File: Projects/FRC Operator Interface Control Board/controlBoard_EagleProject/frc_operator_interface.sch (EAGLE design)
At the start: 41 parts, among them CN1 1uF, CN2 1uF, CN3 1uF, CN4 1uF, J1 AVR_SPI_PRG_6PTH, J2 ANALOGHEADER, J3 DIGITALIN, J4 DIGITALOUTPUTS, J5 PWMHEADER, J6 UE27BC54130-USB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

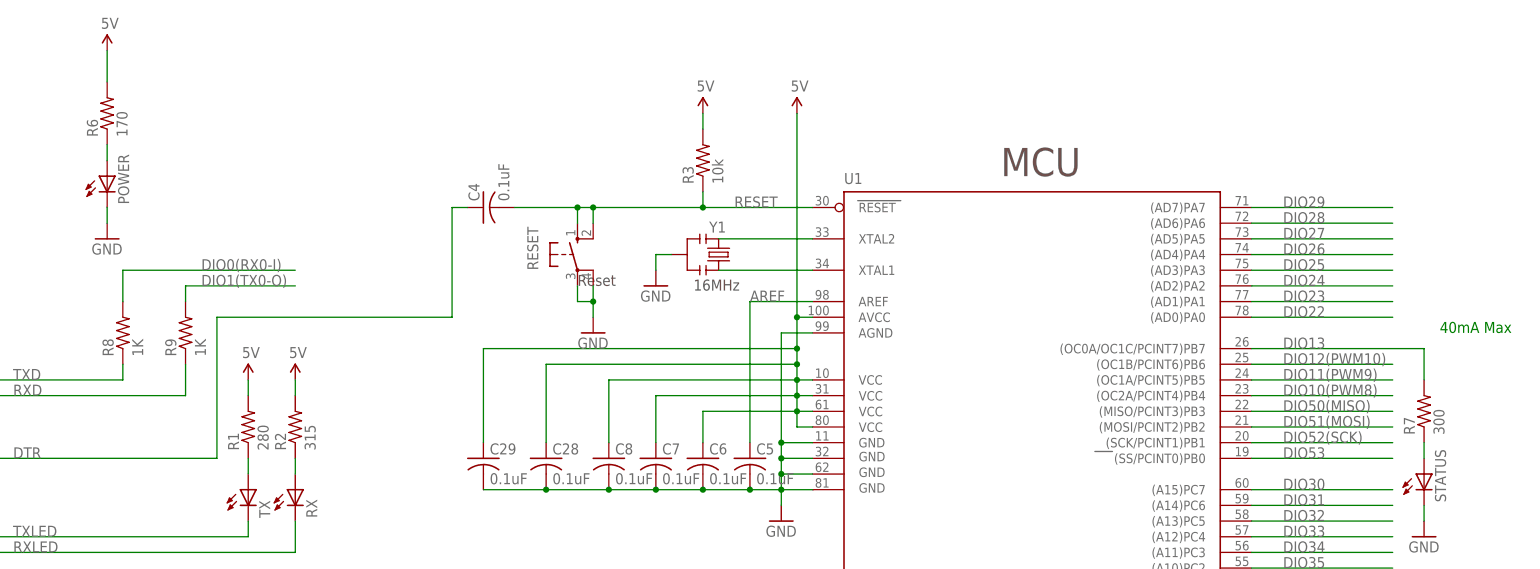
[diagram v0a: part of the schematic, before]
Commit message: Updated the resistor values for some of the LEDs on the board. Controller board code update commit.
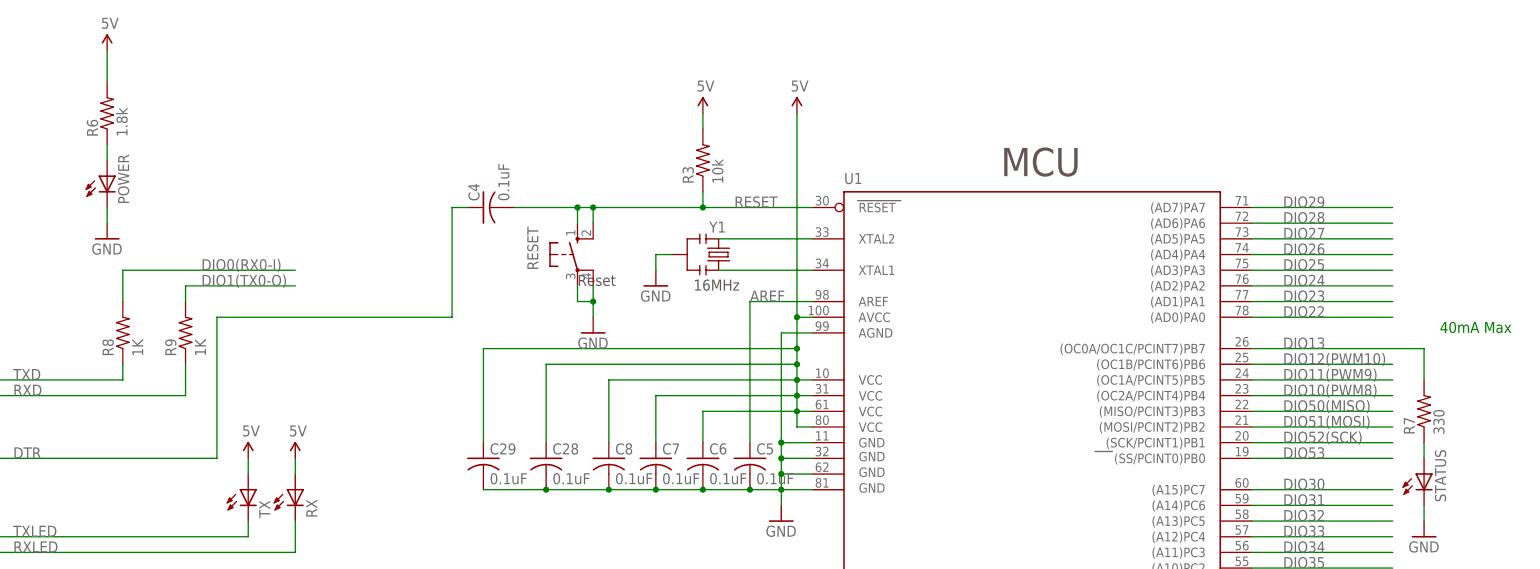
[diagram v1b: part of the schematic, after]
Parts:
- removed R1: 280, rcl:R-US_M1206
- removed R2: 315, rcl:R-US_M1206
- R6: value 170 -> 1.8k
- R7: value 300 -> 330
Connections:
- removed net N$1: R1.1, TX.A
- removed net N$5: R2.1, RX.A
- net 5V: now also RX.A, TX.A; no longer R1.2, R2.2
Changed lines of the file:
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@@
 <?xml version="1.0" encoding="utf-8"?>
 <!DOCTYPE eagle SYSTEM "eagle.dtd">
-<eagle version="6.5.0">
+<eagle version="7.5.0">
 <drawing>
 <settings>
@@
 <part name="C7" library="rcl" deviceset="C-US" device="C1206" value="0.1uF"/>
 <part name="C8" library="rcl" deviceset="C-US" device="C1206" value="0.1uF"/>
-<part name="R6" library="rcl" deviceset="R-US_" device="M1206" value="170"/>
+<part name="R6" library="rcl" deviceset="R-US_" device="M1206" value="1.8k"/>
 <part name="POWER" library="SparkFun-LED" deviceset="LED" device="3MM"/>
 <part name="GND12" library="SparkFun" deviceset="GND" device=""/>
-<part name="R7" library="rcl" deviceset="R-US_" device="M1206" value="300"/>
+<part name="R7" library="rcl" deviceset="R-US_" device="M1206" value="330"/>
 <part name="STATUS" library="SparkFun-LED" deviceset="LED" device="3MM"/>
 <part name="GND13" library="SparkFun" deviceset="GND" device=""/>
@@
 <part name="GND16" library="SparkFun" deviceset="GND" device=""/>
 <part name="U2" library="SparkFun" deviceset="FT232RL" device="SSOP"/>
-<part name="R1" library="rcl" deviceset="R-US_" device="M1206" value="280"/>
-<part name="R2" library="rcl" deviceset="R-US_" device="M1206" value="315"/>
 <part name="TX" library="SparkFun-LED" deviceset="LED" device="3MM"/>
 <part name="RX" library="SparkFun-LED" deviceset="LED" device="3MM"/>
@@
 <instance part="GND16" gate="1" x="12.7" y="187.96" rot="R180"/>
 <instance part="U2" gate="G$1" x="91.44" y="157.48"/>
-<instance part="R1" gate="G$1" x="147.32" y="167.64" rot="R90"/>
-<instance part="R2" gate="G$1" x="154.94" y="167.64" rot="R90"/>
 <instance part="TX" gate="G$1" x="147.32" y="157.48"/>
 <instance part="RX" gate="G$1" x="154.94" y="157.48"/>
-<instance part="U$3" gate="G$1" x="147.32" y="175.26"/>
+<instance part="U$3" gate="G$1" x="147.32" y="162.56"/>
 <instance part="U$4" gate="G$1" x="60.96" y="180.34"/>
-<instance part="U$5" gate="G$1" x="154.94" y="175.26"/>
+<instance part="U$5" gate="G$1" x="154.94" y="162.56"/>
 <instance part="U$6" gate="G$1" x="124.46" y="228.6"/>
 <instance part="U$7" gate="G$1" x="220.98" y="218.44"/>
@@
 </segment>
 </net>
-<net name="N$1" class="0">
-<segment>
-<wire x1="147.32" y1="162.56" x2="147.32" y2="160.02" width="0.1524" layer="91"/>
-<pinref part="R1" gate="G$1" pin="1"/>
-<pinref part="TX" gate="G$1" pin="A"/>
-</segment>
-</net>
-<net name="N$5" class="0">
-<segment>
-<wire x1="154.94" y1="162.56" x2="154.94" y2="160.02" width="0.1524" layer="91"/>
-<pinref part="R2" gate="G$1" pin="1"/>
-<pinref part="RX" gate="G$1" pin="A"/>
-</segment>
-</net>
 <net name="TXD" class="0">
 <segment>
@@
 <wire x1="60.96" y1="162.56" x2="60.96" y2="167.64" width="0.1524" layer="91"/>
 <junction x="60.96" y="167.64"/>
-</segment>
-<segment>
-<wire x1="147.32" y1="175.26" x2="147.32" y2="172.72" width="0.1524" layer="91"/>
-<pinref part="R1" gate="G$1" pin="2"/>
-<pinref part="U$3" gate="G$1" pin="5V"/>
-</segment>
-<segment>
-<wire x1="154.94" y1="175.26" x2="154.94" y2="172.72" width="0.1524" layer="91"/>
-<pinref part="R2" gate="G$1" pin="2"/>
-<pinref part="U$5" gate="G$1" pin="5V"/>
 </segment>
 <segment>
@@
 <wire x1="137.16" y1="-121.92" x2="137.16" y2="-124.46" width="0.1524" layer="91"/>
 </segment>
-</net>
+<segment>
+<wire x1="147.32" y1="162.56" x2="147.32" y2="160.02" width="0.1524" layer="91"/>
+<pinref part="TX" gate="G$1" pin="A"/>
+<pinref part="U$3" gate="G$1" pin="5V"/>
+</segment>
+<segment>
+<wire x1="154.94" y1="162.56" x2="154.94" y2="160.02" width="0.1524" layer="91"/>
+<pinref part="RX" gate="G$1" pin="A"/>
+<pinref part="U$5" gate="G$1" pin="5V"/>
+</segment>
+</net>
